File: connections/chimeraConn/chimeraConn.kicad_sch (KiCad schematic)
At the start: 5 parts, among them M1 SpeedyBee_Nano_2.4G, M2 ANT Lite, M3 Foxeer M10Q-120 compass, M4 Foxeer Reaper Nano V2 VTx 5.8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

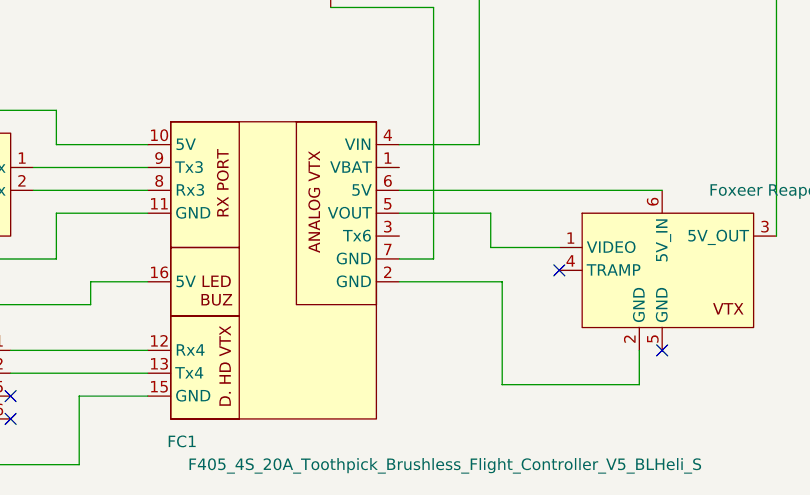
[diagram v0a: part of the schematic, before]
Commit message: update schematic
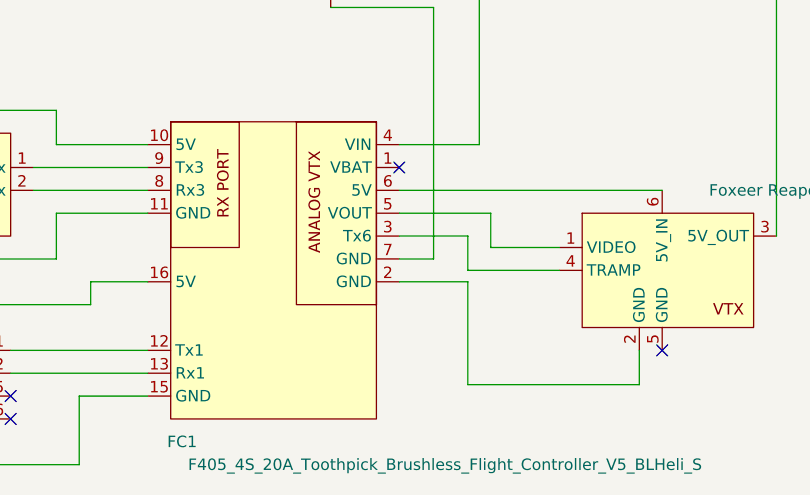
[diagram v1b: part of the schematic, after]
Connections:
- net at M4.4 (TRAMP): now also FC1.3 (Tx6)

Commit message: body redesigned
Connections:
- net at M2.2 (GND): now also M4.5 (GND); no longer FC1.7 (GND)
- no-connect marks 6 -> 5

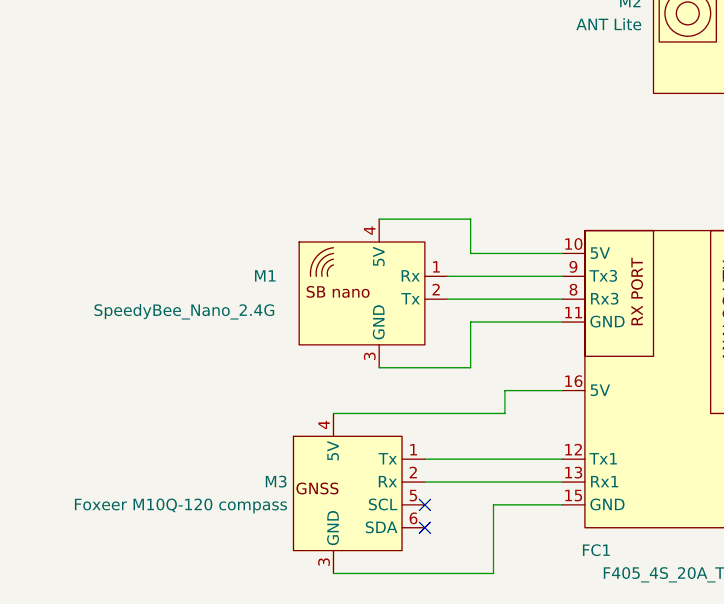
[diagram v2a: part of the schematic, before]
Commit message: update schematic and BOM
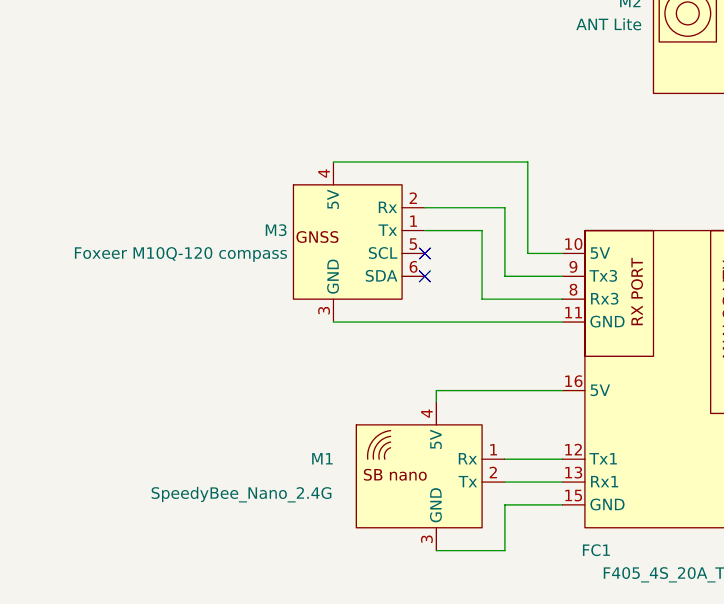
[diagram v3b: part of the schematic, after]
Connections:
- net at M1.1 (Rx): now also FC1.12 (Tx1); no longer FC1.9 (Tx3)
- net at M1.2 (Tx): now also FC1.13 (Rx1); no longer FC1.8 (Rx3)
- net at M1.3 (GND): now also FC1.15 (GND); no longer FC1.11 (GND)
- net at M1.4 (5V): now also FC1.16 (5V); no longer FC1.10 (5V)
- net at M3.1 (Tx): now also FC1.8 (Rx3); no longer FC1.12 (Tx1)
- net at M3.2 (Rx): now also FC1.9 (Tx3); no longer FC1.13 (Rx1)
- net at M3.3 (GND): now also FC1.11 (GND); no longer FC1.15 (GND)
- net at M3.4 (5V): now also FC1.10 (5V); no longer FC1.16 (5V)
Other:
- moved on the sheet: M1, M3

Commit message: new piece of drone
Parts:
- M2: value ANT Lite -> camera

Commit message: add pdf schematic
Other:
- title: (none) -> BD1 "Chimera" connections
